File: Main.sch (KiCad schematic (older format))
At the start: 109 parts, among them U2 MSP430F5529IPN, U3 TPS2557, U4 TPS2557, U5 TPS2557, U6 TPS2557

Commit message: added external charging port
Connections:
- net Cell1/Cell+ renamed EXTERNAL_CHARGER+
- net PACK- renamed EXTERNAL_CHARGER-
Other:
- moved on the sheet: U2
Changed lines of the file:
@@
 L Main-rescue:MSP430F5529IPN-MSP430 U2
 U 1 1 5CC1E5CF
-P 10075 18625
-F 0 "U2" H 12975 19012 60  0000 C CNN
-F 1 "MSP430F5529IPN" H 12975 18906 60  0000 C CNN
-F 2 "PN80" H 12975 18865 60  0001 C CNN
-F 3 "" H 10075 18625 60  0000 C CNN
-	1    10075 18625
+P 17800 18575
+F 0 "U2" H 20700 18962 60  0000 C CNN
+F 1 "MSP430F5529IPN" H 20700 18856 60  0000 C CNN
+F 2 "PN80" H 20700 18815 60  0001 C CNN
+F 3 "" H 17800 18575 60  0000 C CNN
+	1    17800 18575
 	1    0    0    -1
 $EndComp
@@
 Wire Notes Line
 	725  7275 2350 7275
+Text GLabel 6700 6275 1    79   Input ~ 0
+EXTERNAL_CHARGER+
+Text GLabel 6700 7525 3    79   Input ~ 0
+EXTERNAL_CHARGER-
+Wire Wire Line
+	6200 7525 6700 7525
+Connection ~ 6200 7525
+Wire Wire Line
+	6700 6275 6200 6275
+Connection ~ 6200 6275
 $EndSCHEMATC

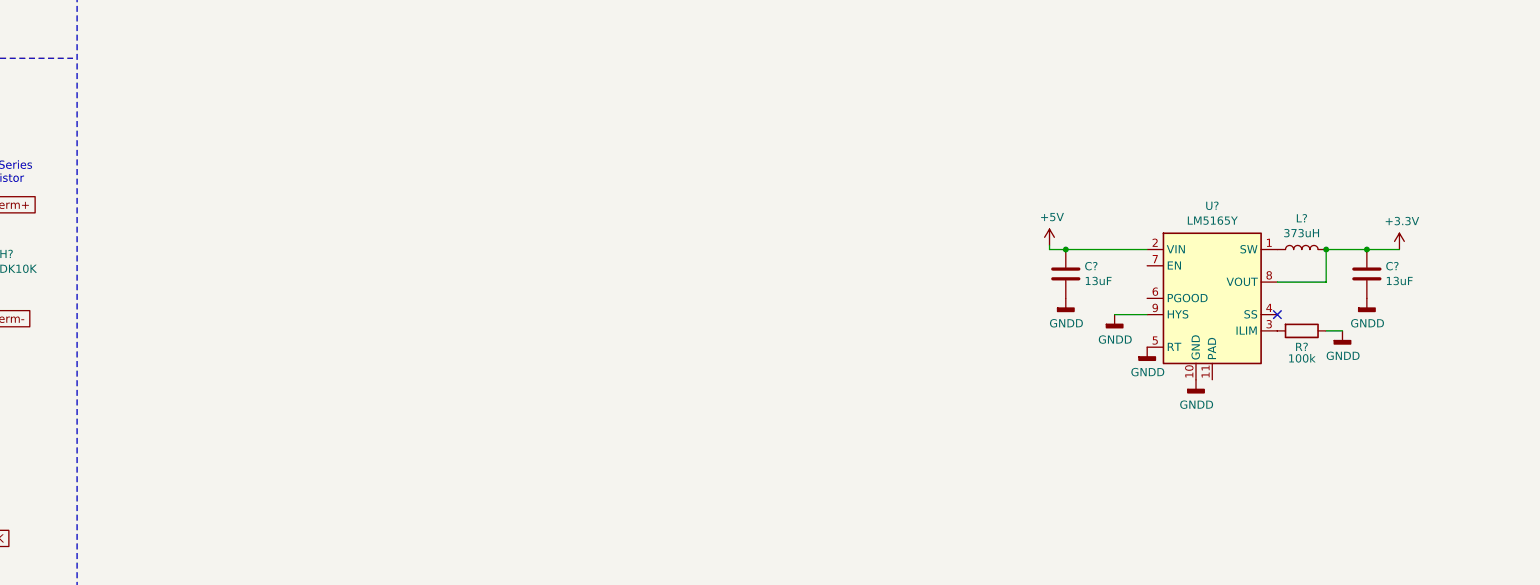
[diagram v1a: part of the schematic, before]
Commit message: added 5v regulator :
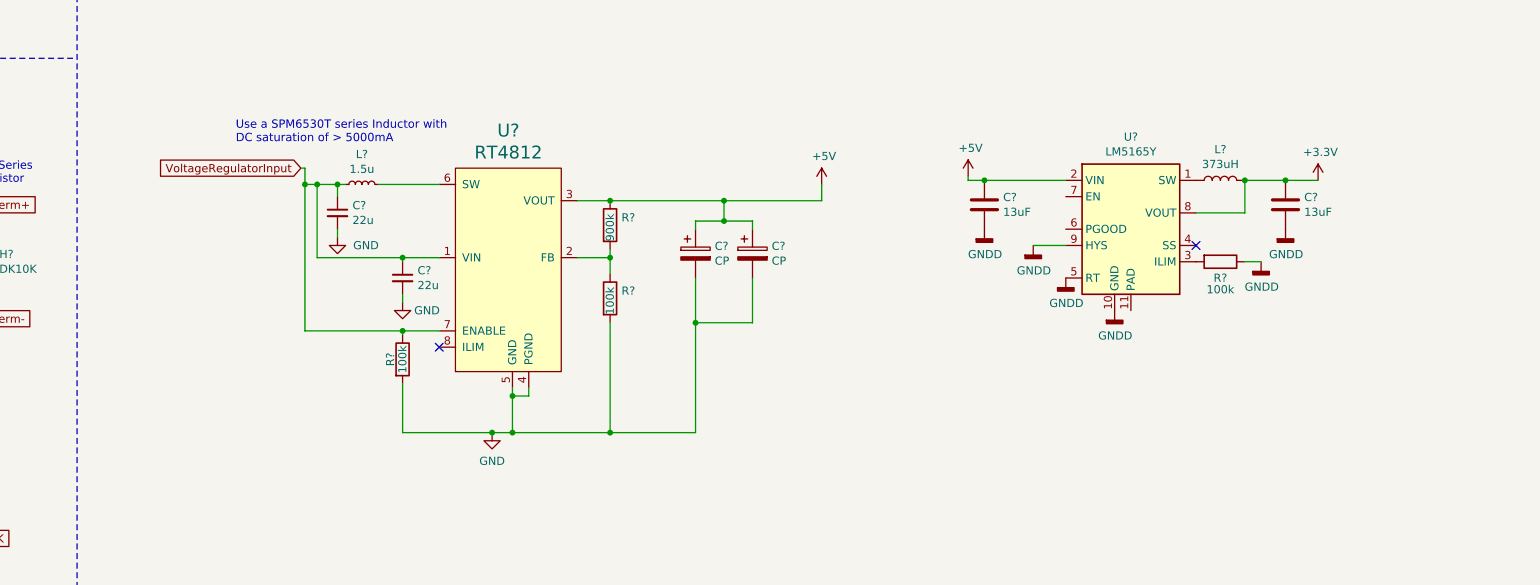
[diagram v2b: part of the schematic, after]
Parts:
- added C? (x2): 22u, symbol Device:C_Small
- added C? (x2): CP, symbol Device:CP
- added L?: 1.5u, symbol Device:L_Small
- added R? (x2): 100k, symbol Device:R
- added R?: 900k, symbol Device:R
- added U?: RT4812, symbol 5v_PowerRegulator_Loris:RT4812
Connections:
- net +5V: now also C?.1, C?.1, R?.1, U?.3 (VOUT)
- net VoltageRegulatorInput: now also C?.1, C?.1, L?.1, R?.1, U?.1 (VIN), U?.7 (ENABLE)
- new net: L?.2, U?.6 (SW)
- new net: R?.1, R?.2, U?.2 (FB)
- new net GND: C?.2, C?.2, C?.2, C?.2, R?.2, R?.2, U?.4 (PGND), U?.5 (GND)
- no-connect marks 18 -> 19
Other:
- note added: "Use a SPM6530T series Inductor with \nDC saturation of > 5000mA"
- moved on the sheet: C?, L?, R?, U?

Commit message: added ground leg inhibit
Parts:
- removed C4: 0.1u, symbol Main-rescue:C-Device
- removed C8: 150u, symbol Main-rescue:C-Device
- removed M?: MNMOS, symbol pspice:MNMOS
- removed R12: TBD, symbol Main-rescue:R_Shunt-Device
- removed R16: R, symbol Main-rescue:R-Device
- removed R?: 100k, symbol Device:R
- removed SW?: RBF Pin, symbol Main-rescue:SW_Push-Switch
- removed U2: MSP430F5529IPN, PN80, symbol Main-rescue:MSP430F5529IPN-MSP430
- removed U6: TPS2557, symbol Main-rescue:TPS2557-CustomSymbols
- removed U? (x6): MAX44284E, symbol MAX44284E:MAX44284E
- added M?: CSD85312Q3E, symbol InhibitSwitches:CSD85312Q3E
- added R?: 100k, symbol Device:R
- added SW?: RBF Switch 1, symbol Main-rescue:SW_Push-Switch
- added SW?: Deployment Switch 3, symbol Main-rescue:SW_Push-Switch
- added U? (x6): MAX44284E, symbol MAX44284E:MAX44284E
- SW?: value Deployment Switch 3 -> RBF Switch 2
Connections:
- net InhibitSwitch1 is gone; now on net PACK+: SW?.2
- net +3V3: now also U?.1 (Vdd), U?.1 (Vdd), U?.1 (Vdd), U?.1 (Vdd), U?.1 (Vdd), U?.1 (Vdd), U?.1 (Vdd)
- net +5V: no longer U?.1 (Vdd)
- net EXTERNAL_CHARGER-: now also M?.1 (D1), M?.2 (D1), M?.3 (D1)
- net GNDD: now also SW?.1, M?.6 (D2), M?.7 (D2), M?.8 (D2), U?.2 (GND), U?.2 (GND), U?.2 (GND), U?.2 (GND), U?.2 (GND), U?.2 (GND)
- net PACK+: no longer SW?.1
- net at M?.2 (G), R?.2: now also SW?.2; no longer SW?.2
- net ACS+ renamed 5vACS+
- net 5vACS+: no longer R?.2
- net ACS- renamed 5vACS-
- net 5vACS-: no longer R?.3
- net ACS_ADC renamed 5vACS_ADC
- net OBC+ renamed 3v3OBC+
- net 3v3OBC+: now also U?.3 (RS+), U?.3 (RS+); no longer R9.2
- net OBC- renamed 3v3OBC-
- net 3v3OBC-: now also U?.6 (RS-), U?.6 (RS-); no longer R9.3
- net PAYLOAD+ renamed 3v3PAYLOAD+
- net 3v3PAYLOAD+: no longer R10.2
- net PAYLOAD- renamed 3v3PAYLOAD-
- net 3v3PAYLOAD-: no longer R10.3
- net RF+ renamed 3v3RF+
- net 3v3RF+: now also U?.3 (RS+)
- net RF- renamed 3v3RF-
- net 3v3RF-: now also U?.6 (RS-)
- net ~ACS_SHDN renamed ~5vACS_SHDN
- new net: SW?.1, SW?.2 (x2)
- new net: M?.5 (Common_Source), R?.2, SW?.1
- new net: M?.5 (Common_Source), R?.1
- new net 3v3ACS+: R?.2, U?.3 (RS+)
- new net 3v3ACS-: R?.3, U?.6 (RS-)
- new net 3v3ACS_ADC: U?.5 (OUT)
- new net 3v3OBC_ADC: U?.5 (OUT)
- new net 3v3PAYLOAD_ADC: U?.5 (OUT)
- new net 3v3RF_ADC: U?.5 (OUT)
- new net 5vOBC+: R9.2, U?.3 (RS+), U?.3 (RS+)
- new net 5vOBC-: R9.3, U?.6 (RS-), U?.6 (RS-)
- new net 5vOBC_ADC: U?.5 (OUT)
- new net 5vPAYLOAD+: R10.2
- new net 5vPAYLOAD-: R10.3
- new net 5vPAYLOAD_ADC: U?.5 (OUT)
- new net ~3v3ACS_SHDN: U?.4 (~SHDN)
- new net ~3v3OBC_SHDN: U?.4 (~SHDN)
- new net ~3v3PAYLOAD_SHDN: U?.4 (~SHDN)
- new net ~3v3RF_SHDN: U?.4 (~SHDN)
- new net ~5vOBC_SHDN: U?.4 (~SHDN)
- new net ~5vPAYLOAD_SHDN: U?.4 (~SHDN)
- no-connect marks 19 -> 18
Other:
- note added: "All switches are mom-off"
- note added: "Both switches are mom-off."
- note removed: "RBF Mechanism\nmom-off \n(when pin is in switch is open)"
- note removed: "Roller Switch\nmom-off"
- note removed: "Tactical Switch\nmom-off"
- moved on the sheet: SW?, U?

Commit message: changed mosfets in inhibit
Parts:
- removed M? (x2): MPMOS-pspice, symbol Main-rescue:MPMOS-pspice
- removed M?: MNMOS, symbol pspice:MNMOS
- removed M?: CSD85312Q3E, symbol InhibitSwitches:CSD85312Q3E
- removed M?: MPMOS, symbol pspice:MPMOS
- removed R?: 284k, symbol Device:R
- removed R?: 100k, symbol Device:R
- removed SW?: Deployment Switch 1, symbol Main-rescue:SW_Push-Switch
- removed SW?: RBF Switch 1, symbol Main-rescue:SW_Push-Switch
- removed U?: LM393, symbol Main-rescue:LM393
- removed U?: SN74LVC2G08, symbol Main-rescue:SN74LVC2G08
- added M? (x3): Si7137DP, symbol InhibitSwitches:Si7137DP
- added Q? (x3): BSB013NE2LXI, Package_DirectFET:DirectFET_MX, symbol Transistor_FET:BSB013NE2LXI
- added R?: 500k, symbol Device:R
- added SW?: Deployment Switch 1, symbol Main-rescue:SW_Push-Switch
- added SW?: RBF Switch 1, symbol Main-rescue:SW_Push-Switch
- R? (x3): value 100k -> 500k
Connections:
- net UnregulatedPreInhibit is gone; now on net MPB: R?.1
- net EXTERNAL_CHARGER-: now also Q?.1 (D)
- net GND: now also Q?.1 (D)
- net GNDD: now also U?.11 (PAD), Q?.3 (S)
- net MPB: now also C?.1, D?.1 (K), R?.4, U?.2 (IN), U?.3 (IN), M?.1 (S), M?.2 (S), M?.3 (S); no longer R?.1
- net PACK+: now also SW?.2
- net VoltageRegulatorInput: now also M?.5 (D)
- net at R?.1: now also M?.1 (S), M?.2 (S), M?.3 (S), M?.5 (D)
- net at R?.2, SW?.2: now also M?.~ (G) (x2)
- net at R?.1, R?.1, U?.5 (V+): now also M?.1 (S), M?.2 (S), M?.3 (S), M?.5 (D)
- net at R?.2: now also M?.~ (G), Q?.1 (D)
- net at R?.1, R?.1, U?.6 (OUT): now also Q?.2 (G)
- new net: SW?.1, SW?.2
- new net: Q?.2 (G), Q?.2 (G), R?.1, SW?.1
- new net: Q?.3 (S), Q?.3 (S), R?.2
- new net X+/OUT+: R?.1
- no-connect marks 18 -> 17
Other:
- note removed: "AND Gate"
- moved on the sheet: C?, L?, R?, TH?, U?

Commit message: added burn wire load switches
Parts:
- removed C? (x2): CP, symbol Device:CP
- removed R? (x3): 887k, symbol Device:R
- removed R?: 4.87k, symbol Device:R
- removed R?: 28k, symbol Device:R
- removed TH?: TDK10K, symbol Device:Thermistor
- removed U? (x7): MAX44284E, symbol MAX44284E:MAX44284E
- added C151, C152, C153, C154, C155, C156, C157, C158: 10u, symbol Device:C_Small
- added C24, C25: 22u, symbol Device:CP1
- added C27, C29: 1u, symbol Device:C
- added R164, R25, R26, R30: Rlim, symbol Device:R
- added R165, R166, R27, R29: BurnWire, symbol Device:Heater
- added R46, R50: 1M, symbol Device:R
- added R47, R51: 887k, symbol Device:R
- added R48, R52: 715k, symbol Device:R
- added U16: LTC6993xS6-1, Package_TO_SOT_SMD:TSOT-23-6, symbol Timer:LTC6993xS6-1
- added U17: LTC6993xS6-3, Package_TO_SOT_SMD:TSOT-23-6, symbol Timer:LTC6993xS6-3
- added U57, U58, U59, U60: AP22653, symbol Main-rescue:AP22653
- gave numbers to parts that had none: 81
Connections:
- net +5V: now also U15.7 (EN), C151.1, C152.1, C153.1, C154.1, C155.1, C156.1, C157.1, C158.1, C24.1, C25.1, U57.1 (IN), U58.1 (IN), U59.1 (IN), U60.1 (IN)
- net GND: no longer Q2.1 (D), R38.2, R42.2, U13.4 (PGND), U13.5 (GND)
- net GNDD: now also Q2.1 (D), R38.2, R42.2, U13.4 (PGND), U13.5 (GND), C151.2, C152.2, C153.2, C154.2, C155.2, C156.2, C157.2, C158.2, C24.2, C25.2, C27.2, C29.2, R164.2, R165.2, R166.2, R25.2, R26.2, R27.2, R29.2, R30.2, R47.2, R48.2, R51.2, R52.2, U16.2 (GND), U17.2 (GND), U57.2 (GND), U58.2 (GND), U59.2 (GND), U60.2 (GND)
- net VoltageRegulatorInput: now also C27.1, C29.1, R46.1, R50.1, U16.1 (TRIG), U16.5 (V+), U17.5 (V+)
- new net: R48.1, U16.3 (SET)
- new net: R46.2, R47.1, U16.4 (DIV)
- new net: R52.1, U17.3 (SET)
- new net: R50.2, R51.1, U17.4 (DIV)
- new net: R25.1, U57.5 (ILIM)
- new net: R27.1, U57.6 (OUT)
- new net: R26.1, U58.5 (ILIM)
- new net: R29.1, U58.6 (OUT)
- new net: R30.1, U59.5 (ILIM)
- new net: R165.1, U59.6 (OUT)
- new net: R164.1, U60.5 (ILIM)
- new net: R166.1, U60.6 (OUT)
- new net FirstBurn: U16.6 (OUT), U17.1 (TRIG), U57.3 (EN), U58.3 (EN)
- new net SecondBurn: U17.6 (OUT), U59.3 (EN), U60.3 (EN)
- no-connect marks 17 -> 22
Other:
- note added: "Burn Wire Load Switches."
- note added: "Current Sensing Op Amps (Will be selected once closer to flatsat)"
- note added: "Ground Leg Inhibit Switch"
- note added: "Inhibit Switches, RBF pin, 30 minute timer\nBurn Wire Timer"
- note added: "Notes:\n1. The LTC6993-1 (U16) is configured as a 30 second monostable that will trigger on a rising edge.\n2. The LTC6993-3 (U17) is configured as a 30 second monostable that will trigger on a falling edge.\n3. The ouput of the two 30s timers control the burn wire load switch.\n4. The LTC6995-1 (U14) is the 30 minute timer."
- note added: "Notes:\n1. The resistor in series with load switch will be fed to a amplifier.\n2. The resistors attached to ILIM will be set to limit 150% of max current\n for each load.\n3. The resistor value for limiting the current through the burn wire \n will be done through extensive testing.\n"
- note added: "Notes:\nDischargeOK HIGH when Vbat is > 2.8 V\nChargeOK HIGH when Vbat is < 4.2 V"
- note added: "X- and X+"
- note added: "Y- and Y+"
- note removed: "Current Sensing Op Amps"
- note removed: "Inhibit Switch 1"
- note removed: "Inhibit Switches, RBF pin and 30 minute timer"
- note removed: "NTCG Series \nThermistor"
- moved on the sheet: C1, C11, C12, C13, C14, C17, C18, C19, C2, C20, C3, C5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
